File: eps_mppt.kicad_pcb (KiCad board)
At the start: 2 copper layers, 34.2 x 23.4 mm, 23 parts, among them J1 PV_IN, J2 OUT, U1 SPV1040, U2 ACS725xLCTR-10AU

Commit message: Tweaked layout
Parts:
- moved C3 0.13 mm to (125.6, 113.4)

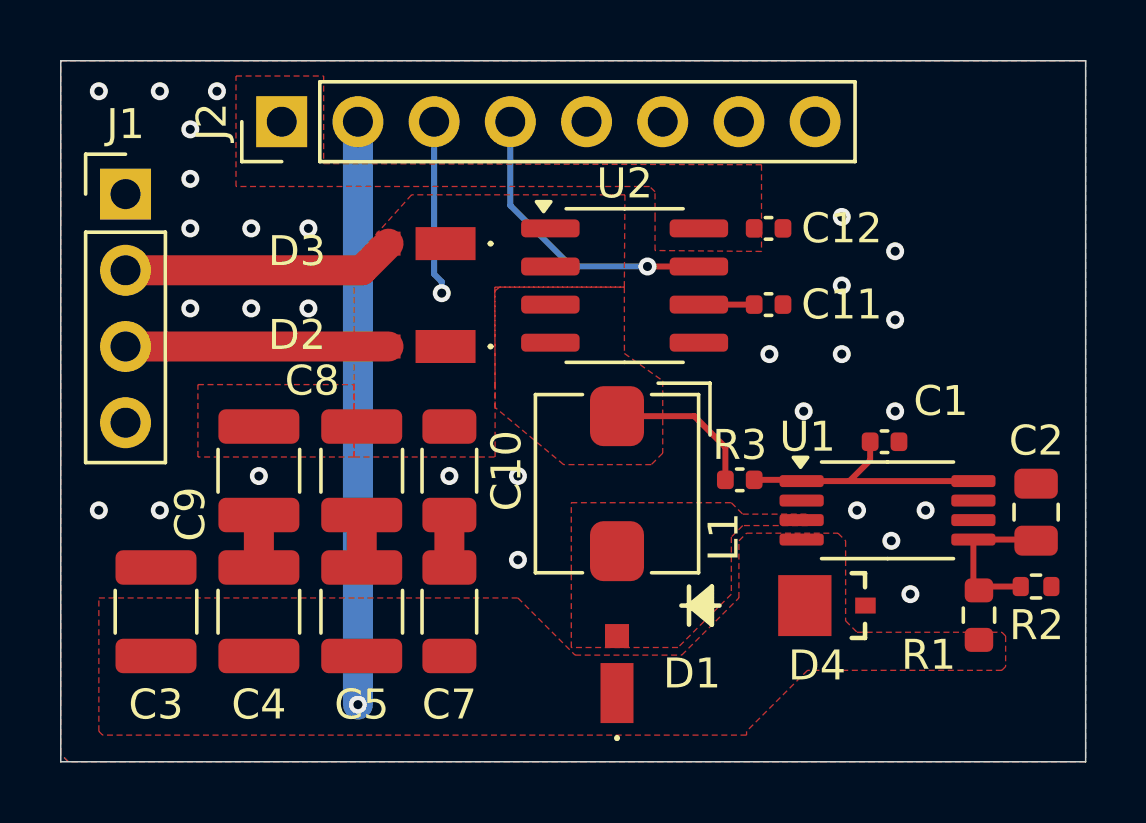
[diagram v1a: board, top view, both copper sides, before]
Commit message: Optimized layout, truncated board
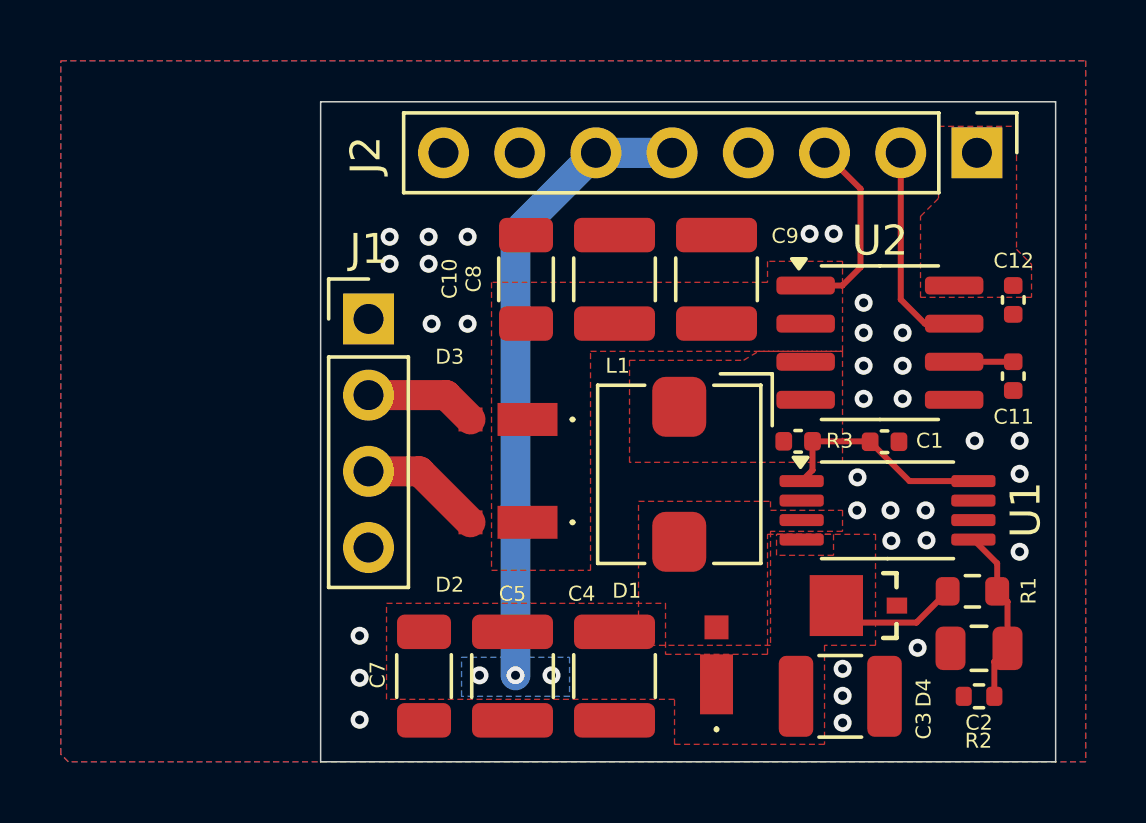
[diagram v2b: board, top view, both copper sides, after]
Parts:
- moved J2 23.2 mm to (153.0, 98.1), turned to -90 degrees
- moved C3 23.0 mm to (148.4, 116.2), turned to 0 degrees
- moved C9 16.5 mm to (144.3, 102.3), turned to -90 degrees
- moved C4 12.0 mm to (140.9, 115.5), turned to -90 degrees
- moved C8 10.6 mm to (140.9, 102.3), turned to -90 degrees
- moved J1 9.11 mm to (132.7, 103.6)
- moved U2 8.72 mm to (149.7, 104.4)
- moved C11 8.50 mm to (154.2, 105.5), turned to -90 degrees
- moved C12 8.50 mm to (154.2, 103.0), turned to -90 degrees
- moved C10 6.87 mm to (137.9, 102.3), turned to -90 degrees
- moved D2 6.47 mm to (137.3, 110.4)
- moved D3 6.47 mm to (137.3, 107.0)
- moved C5 5.46 mm to (137.5, 115.5), turned to -90 degrees
- moved C2 4.92 mm to (153.1, 114.6), turned to 180 degrees
- moved R2 4.12 mm to (153.1, 116.2), turned to 180 degrees
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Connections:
- J2 pad 2: /VOUT -> /PV_CURR
- J2 pad 4: /PV_CURR -> GND
- J2 pad 5: GND -> /VOUT
- J2 pad 6: GND -> /VOUT
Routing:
- net /VOUT: track 19.4 -> 25.4 mm, vias 1 -> 3
- net /PANEL_1: track 9.14 -> 3.74 mm
- net GND: track 5.25 -> 0.00 mm, vias 29 -> 33
- net /PV_LX: track 5.13 -> 0.00 mm
- net /PANEL_2: track 8.77 -> 4.10 mm
- net /PV_CURR: track 9.92 -> 7.00 mm, vias 1 -> 0
- net Net-(U1-MPP_SET): track 8.86 -> 7.39 mm
- net Net-(U1-VCTRL): track 4.83 -> 5.88 mm
- net /PV_VOLT: track 5.82 -> 6.40 mm, vias 1 -> 0
- added copper zone on B.Cu, net /VOUT
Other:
- board size 34.2 x 23.4 mm -> 24.5 x 22 mm

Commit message: Copper fill optimization
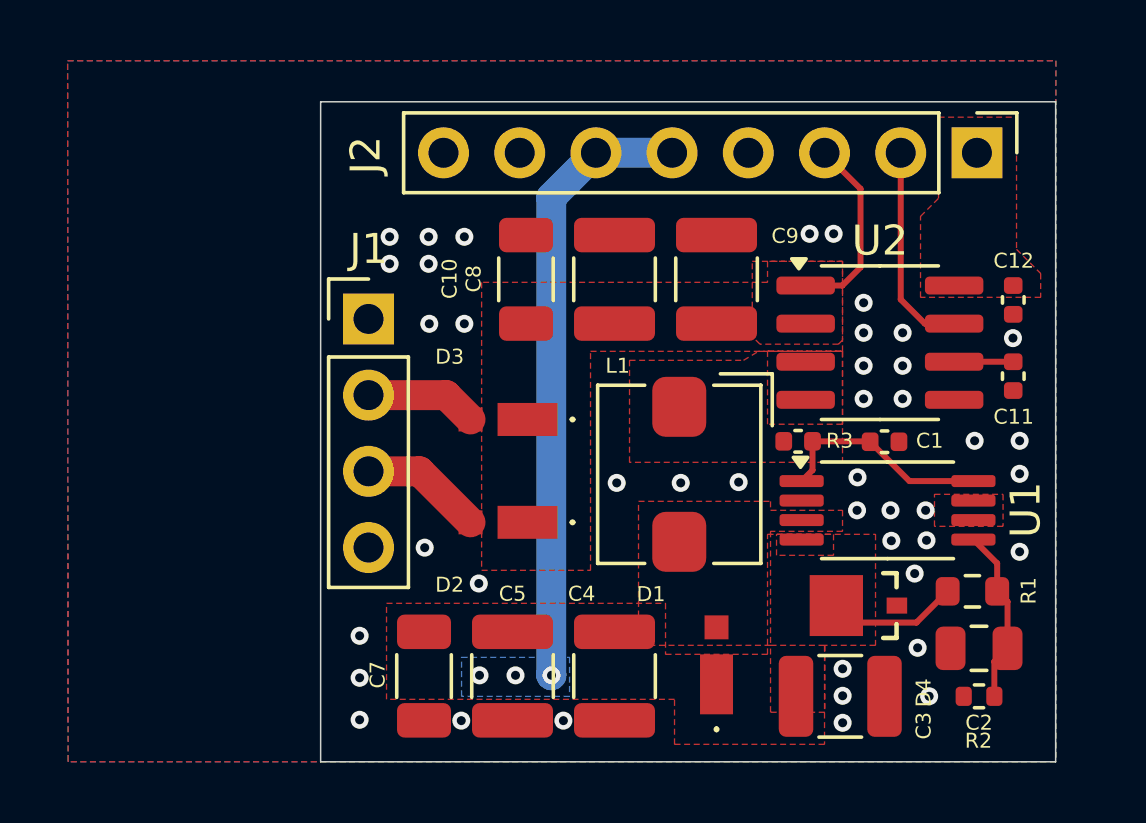
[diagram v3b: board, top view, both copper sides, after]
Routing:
- net GND: vias 33 -> 43
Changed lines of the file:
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@@
 		(tags "capacitor")
 		(property "Reference" "C8"
-			(at -0.018 4.696 270)
+			(at -0.018 4.696 -90)
 			(layer "F.SilkS")
 			(effects
@@
 		(tags "Schottky Diode")
 		(property "Reference" "D1"
-			(at 2.468 -2.996 0)
+			(at 2.356 -2.1834 0)
 			(layer "F.SilkS")
 			(effects
@@
 		)
 		(property "Value" "PD3S220L-7"
-			(at 0 0 270)
+			(at 0 0 -90)
 			(layer "F.SilkS")
 			(hide yes)
@@
 		)
 		(fp_text user "${REFERENCE}"
-			(at 0 0 270)
+			(at 0 0 -90)
 			(layer "F.Fab")
 			(effects
@@
 		(tags "capacitor")
 		(property "Reference" "C7"
-			(at -0.043 1.546 270)
+			(at -0.043 1.546 -90)
 			(layer "F.SilkS")
 			(effects
@@
 		)
 		(property "Value" "1M"
-			(at 0 1.43 360)
+			(at 0 1.43 0)
 			(layer "F.Fab")
 			(effects
@@
 		)
 		(fp_text user "${REFERENCE}"
-			(at 0 0 360)
+			(at 0 0 0)
 			(layer "F.Fab")
 			(effects
@@
 		)
 		(property "Value" "33u"
-			(at -0.039 0.187 270)
+			(at -0.039 0.187 -90)
 			(layer "F.Fab")
 			(effects
@@
 		)
 		(property "Value" "100u"
-			(at 0 2.3 360)
+			(at 0 2.3 0)
 			(layer "F.Fab")
 			(effects
@@
 		)
 		(fp_text user "${REFERENCE}"
-			(at 0 0 360)
+			(at 0 0 0)
 			(layer "F.Fab")
 			(effects
@@
 		)
 		(property "Value" "1k"
-			(at 0 1.16 360)
+			(at 0 1.16 0)
 			(layer "F.Fab")
 			(effects
@@
 		)
 		(fp_text user "${REFERENCE}"
-			(at 0 0 360)
+			(at 0 0 0)
 			(layer "F.Fab")
 			(effects
@@
 	)
 	(via
+		(at 136.3762 112.4384)
+		(size 0.6)
+		(drill 0.3)
+		(layers "F.Cu" "B.Cu")
+		(free yes)
+		(net 1)
+	)
+	(via
+		(at 140.9736 109.0856)
+		(size 0.6)
+		(drill 0.3)
+		(layers "F.Cu" "B.Cu")
+		(free yes)
+		(net 1)
+	)
+	(via
 		(at 132.404 116.982)
 		(size 0.6)
@@
 	)
 	(via
+		(at 150.905 112.1082)
+		(size 0.6)
+		(drill 0.3)
+		(layers "F.Cu" "B.Cu")
+		(free yes)
+		(net 1)
+	)
+	(via
 		(at 132.404 115.582)
 		(size 0.6)
@@
 	)
 	(via
+		(at 145.0376 109.0602)
+		(size 0.6)
+		(drill 0.3)
+		(layers "F.Cu" "B.Cu")
+		(free yes)
+		(net 1)
+	)
+	(via
 		(at 154.404 107.682)
 		(size 0.6)
@@
 	)
 	(via
+		(at 135.792 117.0104)
+		(size 0.6)
+		(drill 0.3)
+		(layers "F.Cu" "B.Cu")
+		(free yes)
+		(net 1)
+	)
+	(via
 		(at 133.404 101.782)
 		(size 0.6)
@@
 	)
 	(via
-		(at 136.004 100.882)
+		(at 135.8936 100.882)
 		(size 0.6)
 		(drill 0.3)
@@
 	)
 	(via
-		(at 134.804 103.782)
+		(at 134.7252 103.782)
 		(size 0.6)
 		(drill 0.3)
@@
 	)
 	(via
+		(at 154.1816 104.2596)
+		(size 0.6)
+		(drill 0.3)
+		(layers "F.Cu" "B.Cu")
+		(free yes)
+		(net 1)
+	)
+	(via
 		(at 149.204 103.082)
 		(size 0.6)
@@
 	)
 	(via
+		(at 143.1072 109.0856)
+		(size 0.6)
+		(drill 0.3)
+		(layers "F.Cu" "B.Cu")
+		(free yes)
+		(net 1)
+	)
+	(via
+		(at 139.1956 117.0104)
+		(size 0.6)
+		(drill 0.3)
+		(layers "F.Cu" "B.Cu")
+		(free yes)
+		(net 1)
+	)
+	(via
 		(at 132.404 114.182)
 		(size 0.6)
@@
 	)
 	(via
+		(at 134.5728 111.2446)
+		(size 0.6)
+		(drill 0.3)
+		(layers "F.Cu" "B.Cu")
+		(free yes)
+		(net 1)
+	)
+	(via
 		(at 148.504 117.082)
 		(size 0.6)
@@
 	)
 	(via
-		(at 136.004 103.782)
+		(at 135.8936 103.782)
 		(size 0.6)
 		(drill 0.3)
@@
 	)
 	(via
+		(at 151.3876 116.1976)
+		(size 0.6)
+		(drill 0.3)
+		(layers "F.Cu" "B.Cu")
+		(free yes)
+		(net 1)
+	)
+	(via
 		(at 154.404 111.382)
 		(size 0.6)
@@
 	)
 	(segment
-		(start 137.6 100.762)
+		(start 138.7892 115.4892)
+		(end 138.7892 99.5728)
+		(width 1)
+		(layer "B.Cu")
+		(net 4)
+	)
+	(segment
+		(start 138.7892 99.5728)
 		(end 140.28 98.082)
 		(width 1)
@@
 	)
 	(segment
-		(start 137.6 115.5)
-		(end 137.6 100.762)
+		(start 138.8 115.5)
+		(end 138.7892 115.4892)
 		(width 1)
 		(layer "B.Cu")
@@
 		(fill yes
 			(thermal_gap 0.254)
-			(thermal_bridge_width 0.508)
+			(thermal_bridge_width 1.016)
 			(smoothing fillet)
 			(radius 0.254)
@@
 		(polygon
 			(pts
-				(xy 148.5 101.7) (xy 146 101.7) (xy 146 102.4) (xy 136.8 102.4) (xy 136.8 112) (xy 140.1 112) (xy 140.1 104.7)
-				(xy 148.5 104.7)
+				(xy 148.5 101.7) (xy 146 101.7) (xy 146 102.4) (xy 136.4698 102.4) (xy 136.4698 112) (xy 140.1 112)
+				(xy 140.1 104.7) (xy 148.5 104.7)
+			)
+		)
+	)
+	(zone
+		(net 12)
+		(net_name "/PV_LX")
+		(layer "F.Cu")
+		(hatch edge 0.5)
+		(priority 8)
+		(connect_pads
+			(clearance 0.1524)
+		)
+		(min_thickness 0.25)
+		(filled_areas_thickness no)
+		(fill yes
+			(thermal_gap 0)
+			(thermal_bridge_width 1)
+		)
+		(polygon
+			(pts
+				(xy 146 104.6972) (xy 148.5 104.6972) (xy 148.5 107.1218) (xy 148.492 107.1298) (xy 146.0028 107.1298)
+				(xy 146 107.127)
 			)
 		)
@@
 		(polygon
 			(pts
-				(xy 151.7 97.2) (xy 154.3 97.2) (xy 154.3 101.3) (xy 154.8 101.8) (xy 154.8 102.9) (xy 151.1 102.9)
-				(xy 151.1 100.2) (xy 151.7 99.6)
+				(xy 151.7 96.8952) (xy 154.3 96.8952) (xy 154.3 101.3) (xy 155.1048 102.1048) (xy 155.1048 102.9)
+				(xy 151.1 102.9) (xy 151.1 100.2) (xy 151.7 99.6)
 			)
 		)
@@
 	)
 	(zone
+		(net 4)
+		(net_name "/VOUT")
+		(layer "F.Cu")
+		(hatch edge 0.5)
+		(priority 10)
+		(connect_pads
+			(clearance 0.1524)
+		)
+		(min_thickness 0.1524)
+		(filled_areas_thickness no)
+		(fill yes
+			(thermal_gap 0)
+			(thermal_bridge_width 1.016)
+			(smoothing fillet)
+			(radius 0.254)
+		)
+		(polygon
+			(pts
+				(xy 146.1 114.5) (xy 147.9 114.5) (xy 147.9078 114.5078) (xy 147.9078 116.731) (xy 146.1044 116.731)
+				(xy 146.1 116.7266)
+			)
+		)
+	)
+	(zone
+		(net 5)
+		(net_name "/PV_VOLT")
+		(layer "F.Cu")
+		(hatch edge 0.5)
+		(priority 8)
+		(connect_pads
+			(clearance 0.1524)
+		)
+		(min_thickness 0.25)
+		(filled_areas_thickness no)
+		(fill yes
+			(thermal_gap 0)
+			(thermal_bridge_width 1)
+		)
+		(polygon
+			(pts
+				(xy 145.492 101.7) (xy 148.5 101.7) (xy 148.5 104.3278) (xy 148.365 104.4628) (xy 145.7488 104.4628)
+				(xy 145.492 104.206)
+			)
+		)
+	)
+	(zone
+		(net 1)
+		(net_name "GND")
+		(layer "F.Cu")
+		(hatch edge 0.5)
+		(priority 9)
+		(connect_pads
+			(clearance 0.1524)
+		)
+		(min_thickness 0.1524)
+		(filled_areas_thickness no)
+		(fill yes
+			(thermal_gap 0)
+			(thermal_bridge_width 1.016)
+			(smoothing fillet)
+			(radius 0.254)
+		)
+		(polygon
+			(pts
+				(xy 151.5654 109.4666) (xy 153.8514 109.4666) (xy 153.8514 110.5334) (xy 151.5654 110.5334)
+			)
+		)
+	)
+	(zone
 		(net 1)
 		(net_name "GND")
@@
 		(fill yes
 			(thermal_gap 0.254)
-			(thermal_bridge_width 0.508)
+			(thermal_bridge_width 1.016)
 			(smoothing fillet)
 			(radius 0.254)
@@
 		(polygon
 			(pts
-				(xy 156.604 95.014) (xy 156.604 118.382) (xy 122.695 118.382) (xy 122.441 118.128) (xy 122.441 95.014)
+				(xy 155.6134 95.014) (xy 155.6134 118.382) (xy 122.695 118.382) (xy 122.6856 118.3566) (xy 122.6696 95.014)
 			)
 		)
